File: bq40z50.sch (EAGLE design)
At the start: 46 parts, among them Q1 6.5A/30V/38mΩ, Q2 6.5A/30V/38mΩ, U1 BQ40Z50RSMTRSM32_1P5X1P5-M

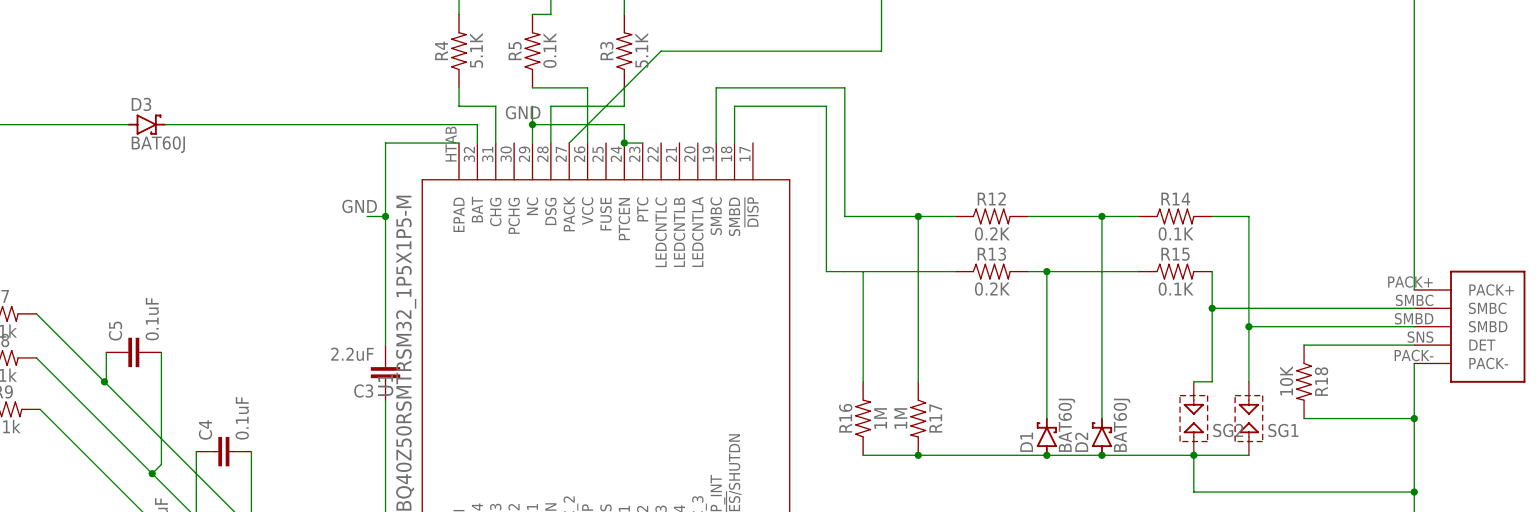
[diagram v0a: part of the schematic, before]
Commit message: schematic : fix reversed SMBC SMBD lines
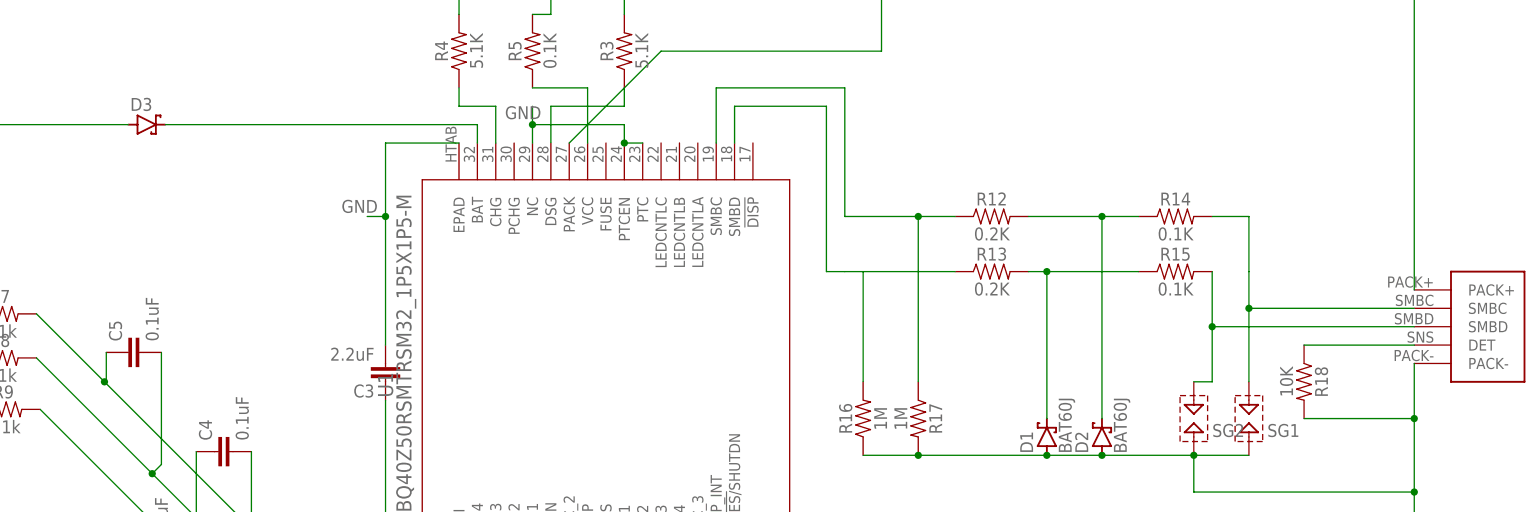
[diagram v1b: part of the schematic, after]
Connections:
- net N$28: now also U$1.SMBD; no longer U$1.SMBC
- net N$29: now also U$1.SMBC; no longer U$1.SMBD
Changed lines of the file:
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@@
 <?xml version="1.0" encoding="utf-8"?>
 <!DOCTYPE eagle SYSTEM "eagle.dtd">
-<eagle version="9.3.0">
+<eagle version="9.4.2">
 <drawing>
 <settings>
@@
 <part name="D1" library="diode" library_urn="urn:adsk.eagle:library:210" deviceset="BAT60J" device="" package3d_urn="urn:adsk.eagle:package:43461/1"/>
 <part name="D2" library="diode" library_urn="urn:adsk.eagle:library:210" deviceset="BAT60J" device="" package3d_urn="urn:adsk.eagle:package:43461/1"/>
-<part name="D3" library="diode" library_urn="urn:adsk.eagle:library:210" deviceset="BAT60J" device="" package3d_urn="urn:adsk.eagle:package:43461/1"/>
+<part name="D3" library="diode" library_urn="urn:adsk.eagle:library:210" deviceset="BAT60J" device="" package3d_urn="urn:adsk.eagle:package:43461/1" value=""/>
 <part name="Q1" library="SparkFun-DiscreteSemi" library_urn="urn:adsk.eagle:library:514" deviceset="MOSFET-NCH" device="-FDS6630A" package3d_urn="urn:adsk.eagle:package:38445/1" value="6.5A/30V/38mΩ"/>
 <part name="Q2" library="SparkFun-DiscreteSemi" library_urn="urn:adsk.eagle:library:514" deviceset="MOSFET-NCH" device="-FDS6630A" package3d_urn="urn:adsk.eagle:package:38445/1" value="6.5A/30V/38mΩ"/>
@@
 <segment>
 <pinref part="R15" gate="G$1" pin="2"/>
-<pinref part="U$1" gate="G$1" pin="SMBC"/>
-<wire x1="218.44" y1="111.76" x2="218.44" y2="106.68" width="0.1524" layer="91"/>
-<wire x1="218.44" y1="106.68" x2="246.38" y2="106.68" width="0.1524" layer="91"/>
-<wire x1="218.44" y1="106.68" x2="218.44" y2="96.52" width="0.1524" layer="91"/>
-<junction x="218.44" y="106.68"/>
+<wire x1="218.44" y1="111.76" x2="218.44" y2="104.14" width="0.1524" layer="91"/>
 <pinref part="SG2" gate="G$1" pin="1"/>
+<wire x1="218.44" y1="104.14" x2="218.44" y2="96.52" width="0.1524" layer="91"/>
 <wire x1="218.44" y1="96.52" x2="215.9" y2="96.52" width="0.1524" layer="91"/>
+<pinref part="U$1" gate="G$1" pin="SMBD"/>
+<wire x1="246.38" y1="104.14" x2="218.44" y2="104.14" width="0.1524" layer="91"/>
+<junction x="218.44" y="104.14"/>
 </segment>
 </net>
 <net name="N$29" class="0">
 <segment>
-<pinref part="U$1" gate="G$1" pin="SMBD"/>
-<wire x1="223.52" y1="104.14" x2="246.38" y2="104.14" width="0.1524" layer="91"/>
 <pinref part="R14" gate="G$1" pin="2"/>
 <wire x1="218.44" y1="119.38" x2="223.52" y2="119.38" width="0.1524" layer="91"/>
-<wire x1="223.52" y1="119.38" x2="223.52" y2="104.14" width="0.1524" layer="91"/>
+<wire x1="223.52" y1="119.38" x2="223.52" y2="111.76" width="0.1524" layer="91"/>
 <pinref part="SG1" gate="G$1" pin="1"/>
-<wire x1="223.52" y1="96.52" x2="223.52" y2="104.14" width="0.1524" layer="91"/>
-<junction x="223.52" y="104.14"/>
-</segment>
-</net>
+<pinref part="U$1" gate="G$1" pin="SMBC"/>
+<wire x1="223.52" y1="106.68" x2="223.52" y2="96.52" width="0.1524" layer="91"/>
+<wire x1="223.52" y1="111.76" x2="223.52" y2="106.68" width="0.1524" layer="91"/>
+<wire x1="223.52" y1="106.68" x2="246.38" y2="106.68" width="0.1524" layer="91"/>
+<junction x="223.52" y="106.68"/>
+</segment>
+</net>

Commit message: schematic : connect FUSE to GND (otherwise 40z50 doesn't enables FETs)
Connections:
- net GND: now also U1.FUSE
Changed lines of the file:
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@@
 <junction x="137.16" y="129.54"/>
 <junction x="124.46" y="132.08"/>
+<pinref part="U1" gate="A" pin="FUSE"/>
+<wire x1="134.62" y1="129.54" x2="137.16" y2="129.54" width="0.1524" layer="91"/>
 </segment>
 <segment>

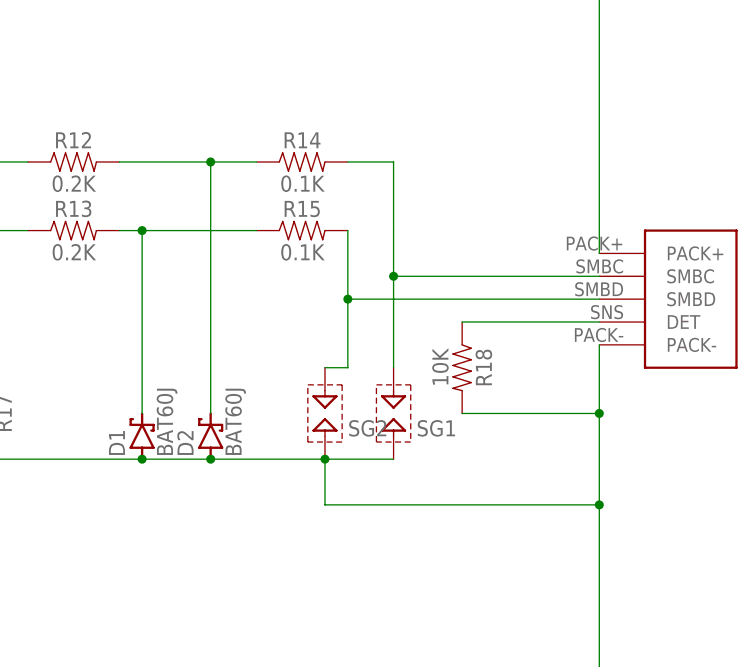
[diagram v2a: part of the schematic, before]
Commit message: schematic : spark gap mod
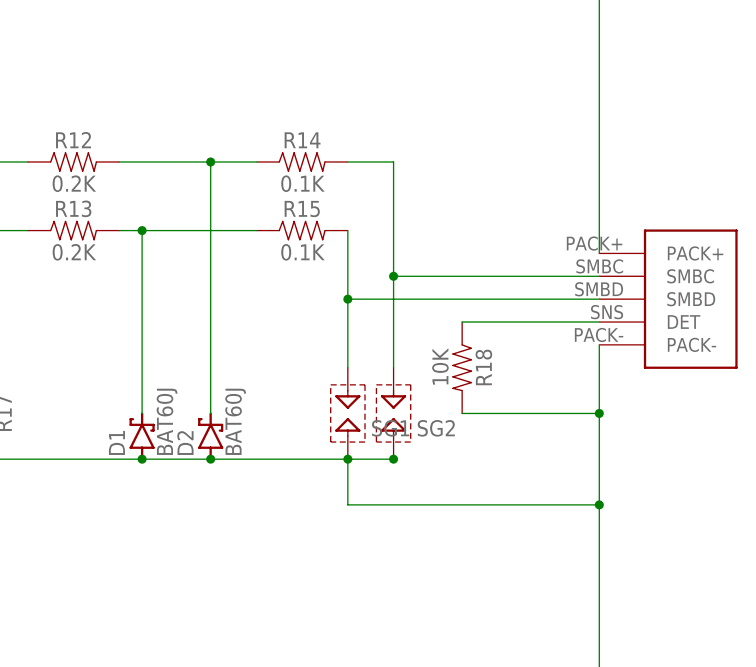
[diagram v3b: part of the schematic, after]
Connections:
- net N$28: now also SG1.1; no longer SG2.1
- net N$29: now also SG2.1; no longer SG1.1
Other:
- moved on the sheet: SG1, SG2
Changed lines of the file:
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@@
 <attribute name="NAME" x="21.844" y="118.11" size="1.27" layer="95" rot="R180" align="center"/>
 </instance>
-<instance part="SG1" gate="G$1" x="223.52" y="91.44" smashed="yes">
+<instance part="SG1" gate="G$1" x="218.44" y="91.44" smashed="yes">
+<attribute name="NAME" x="220.98" y="88.9" size="1.778" layer="95" ratio="10"/>
+</instance>
+<instance part="SG2" gate="G$1" x="223.52" y="91.44" smashed="yes">
 <attribute name="NAME" x="226.06" y="88.9" size="1.778" layer="95" ratio="10"/>
-</instance>
-<instance part="SG2" gate="G$1" x="215.9" y="91.44" smashed="yes">
-<attribute name="NAME" x="218.44" y="88.9" size="1.778" layer="95" ratio="10"/>
 </instance>
 <instance part="R20" gate="G$1" x="88.9" y="172.72" smashed="yes" rot="R180">
@@
 <pinref part="R15" gate="G$1" pin="2"/>
 <wire x1="218.44" y1="111.76" x2="218.44" y2="104.14" width="0.1524" layer="91"/>
-<pinref part="SG2" gate="G$1" pin="1"/>
 <wire x1="218.44" y1="104.14" x2="218.44" y2="96.52" width="0.1524" layer="91"/>
-<wire x1="218.44" y1="96.52" x2="215.9" y2="96.52" width="0.1524" layer="91"/>
 <pinref part="U$1" gate="G$1" pin="SMBD"/>
 <wire x1="246.38" y1="104.14" x2="218.44" y2="104.14" width="0.1524" layer="91"/>
 <junction x="218.44" y="104.14"/>
+<pinref part="SG1" gate="G$1" pin="1"/>
 </segment>
 </net>
@@
 <pinref part="R14" gate="G$1" pin="2"/>
 <wire x1="218.44" y1="119.38" x2="223.52" y2="119.38" width="0.1524" layer="91"/>
-<wire x1="223.52" y1="119.38" x2="223.52" y2="111.76" width="0.1524" layer="91"/>
-<pinref part="SG1" gate="G$1" pin="1"/>
+<wire x1="223.52" y1="119.38" x2="223.52" y2="106.68" width="0.1524" layer="91"/>
 <pinref part="U$1" gate="G$1" pin="SMBC"/>
-<wire x1="223.52" y1="106.68" x2="223.52" y2="96.52" width="0.1524" layer="91"/>
-<wire x1="223.52" y1="111.76" x2="223.52" y2="106.68" width="0.1524" layer="91"/>
 <wire x1="223.52" y1="106.68" x2="246.38" y2="106.68" width="0.1524" layer="91"/>
+<pinref part="SG2" gate="G$1" pin="1"/>
+<wire x1="223.52" y1="96.52" x2="223.52" y2="106.68" width="0.1524" layer="91"/>
 <junction x="223.52" y="106.68"/>
 </segment>
@@
 </segment>
 </net>
-<net name="N$32" class="0">
-<segment>
+<net name="N$3" class="0">
+<segment>
+<pinref part="SG1" gate="G$1" pin="2"/>
+<pinref part="SG2" gate="G$1" pin="2"/>
+<junction x="223.52" y="86.36"/>
+<pinref part="D2" gate="G$1" pin="A"/>
+<wire x1="203.2" y1="86.36" x2="218.44" y2="86.36" width="0.1524" layer="91"/>
+<junction x="203.2" y="86.36"/>
+<pinref part="D1" gate="G$1" pin="A"/>
+<wire x1="218.44" y1="86.36" x2="223.52" y2="86.36" width="0.1524" layer="91"/>
+<wire x1="195.58" y1="86.36" x2="203.2" y2="86.36" width="0.1524" layer="91"/>
+<junction x="195.58" y="86.36"/>
+<pinref part="R17" gate="G$1" pin="2"/>
+<wire x1="177.8" y1="86.36" x2="195.58" y2="86.36" width="0.1524" layer="91"/>
+<junction x="177.8" y="86.36"/>
 <pinref part="R16" gate="G$1" pin="1"/>
-<pinref part="R17" gate="G$1" pin="2"/>
 <wire x1="170.18" y1="86.36" x2="177.8" y2="86.36" width="0.1524" layer="91"/>
-<pinref part="D1" gate="G$1" pin="A"/>
-<pinref part="D2" gate="G$1" pin="A"/>
-<wire x1="195.58" y1="86.36" x2="203.2" y2="86.36" width="0.1524" layer="91"/>
-<pinref part="SG2" gate="G$1" pin="2"/>
-<wire x1="203.2" y1="86.36" x2="215.9" y2="86.36" width="0.1524" layer="91"/>
-<junction x="203.2" y="86.36"/>
-<pinref part="SG1" gate="G$1" pin="2"/>
-<wire x1="215.9" y1="86.36" x2="223.52" y2="86.36" width="0.1524" layer="91"/>
-<junction x="215.9" y="86.36"/>
 <pinref part="SR" gate="G$1" pin="1"/>
 <pinref part="U$1" gate="G$1" pin="PACK-"/>
@@
 <wire x1="231.14" y1="91.44" x2="246.38" y2="91.44" width="0.1524" layer="91"/>
 <junction x="246.38" y="91.44"/>
-<wire x1="215.9" y1="86.36" x2="215.9" y2="81.28" width="0.1524" layer="91"/>
-<wire x1="215.9" y1="81.28" x2="246.38" y2="81.28" width="0.1524" layer="91"/>
+<wire x1="218.44" y1="81.28" x2="246.38" y2="81.28" width="0.1524" layer="91"/>
 <junction x="246.38" y="81.28"/>
-<wire x1="177.8" y1="86.36" x2="195.58" y2="86.36" width="0.1524" layer="91"/>
-<junction x="177.8" y="86.36"/>
-<junction x="195.58" y="86.36"/>
-</segment>
-</net>
+<wire x1="218.44" y1="86.36" x2="218.44" y2="81.28" width="0.1524" layer="91"/>
+<junction x="218.44" y="86.36"/>
+</segment>
+</net>
